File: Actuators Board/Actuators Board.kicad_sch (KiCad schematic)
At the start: 73 parts, among them J1 Conn_01x05_Male, J10 Conn_01x02_Male, J2 Solenoid(Sol), J4 Conn_01x03_Male, J5 Conn_01x06_Male, J9 Conn_01x02_Male, Q1 MMDT2222A, Q2 SI2366DS, U1 ESP32-PICO-D4, U2 TPS54233D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

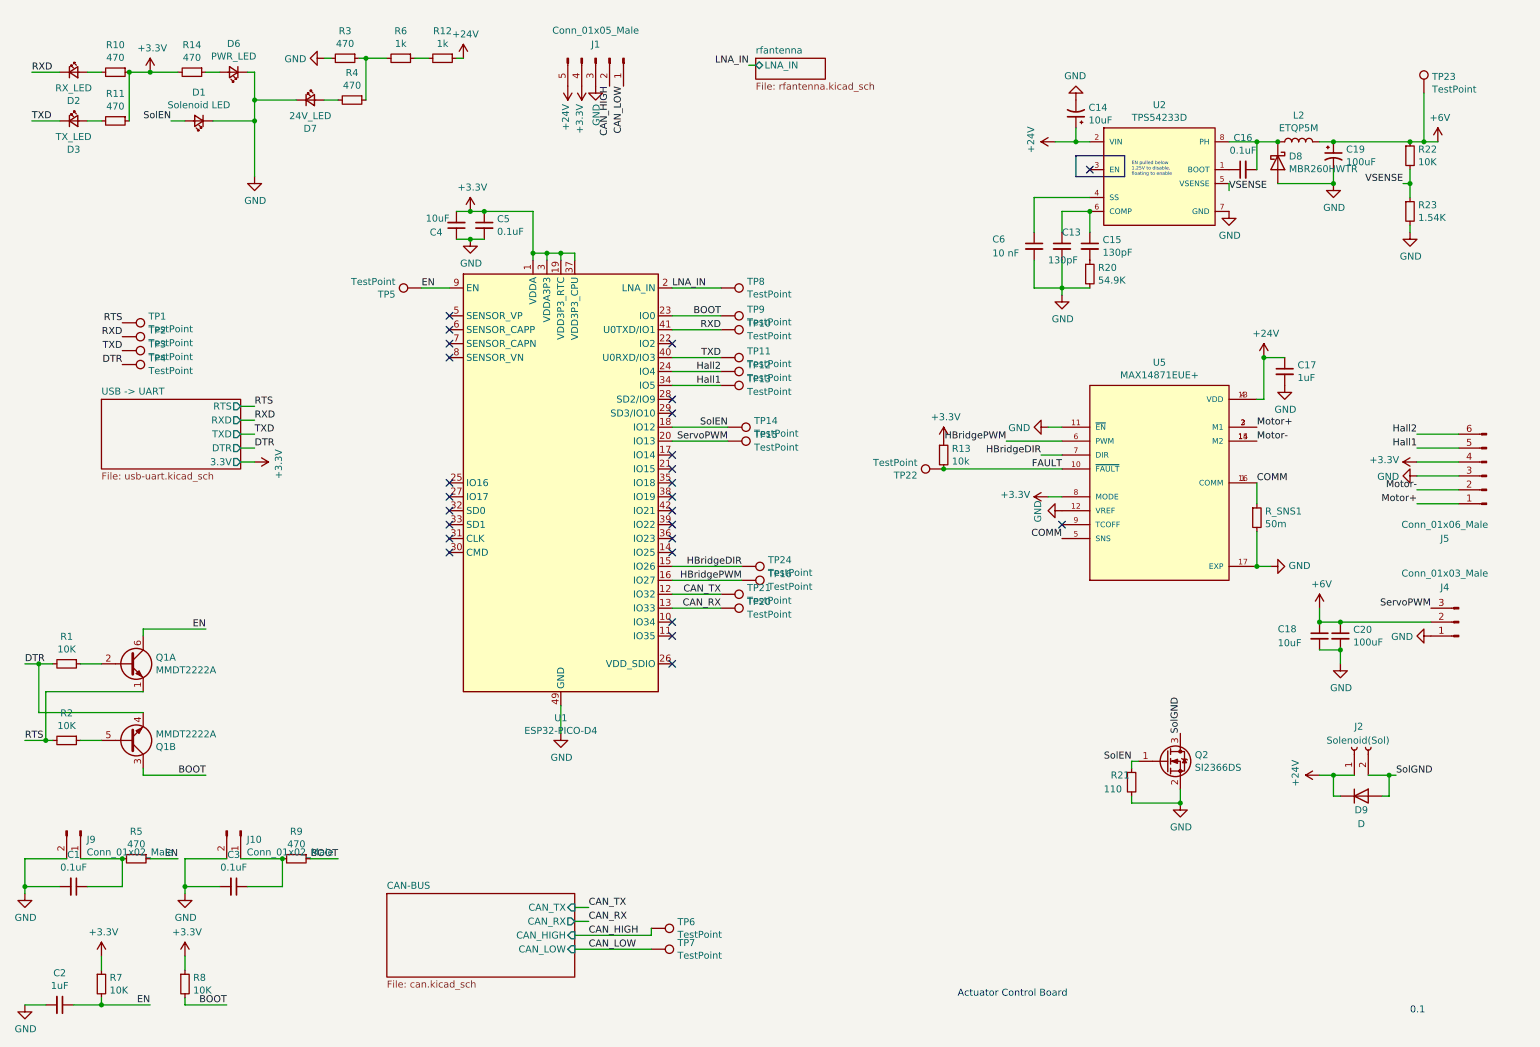
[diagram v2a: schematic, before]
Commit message: Preliminary layout of buck converter & supporting components
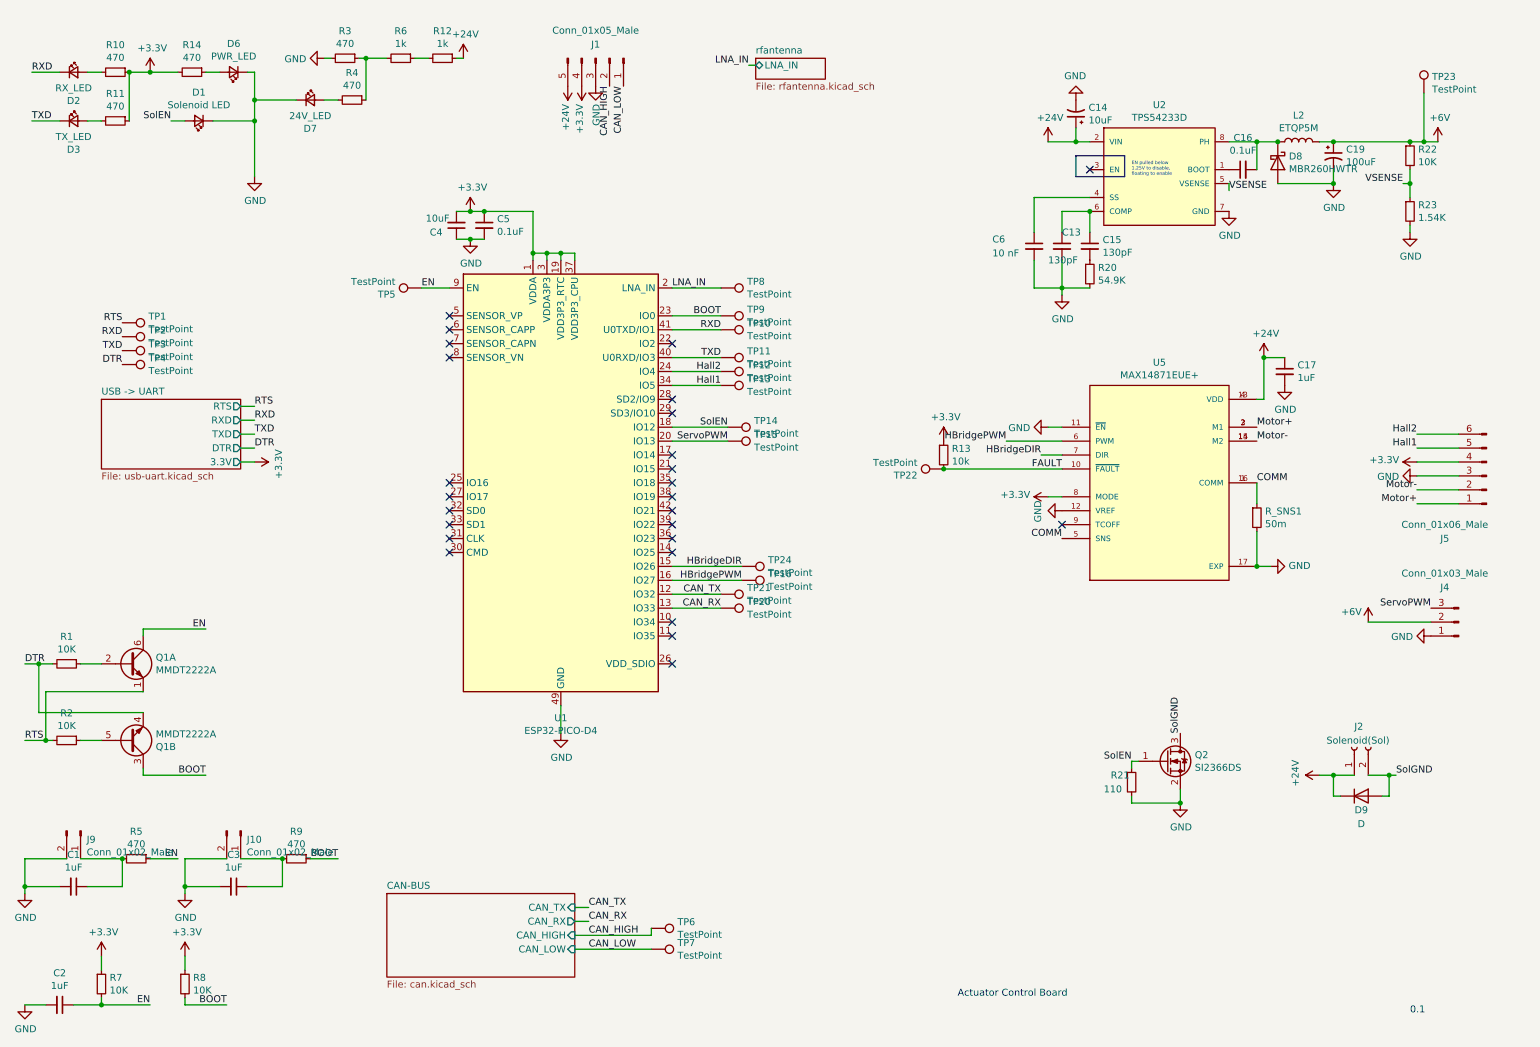
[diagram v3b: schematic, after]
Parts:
- removed C18: 10uF, Capacitor_SMD:C_0603_1608Metric, symbol Device:C_Small
- removed C20: 100uF, Capacitor_SMD:C_0603_1608Metric, symbol Device:C_Small
- C1, C3: value 0.1uF -> 1uF
- J4: footprint (none) -> Connector_JST:JST_XH_B3B-XH-AM_1x03_P2.50mm_Vertical
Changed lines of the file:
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@@
   (junction (at 35.56 21.59) (diameter 0) (color 0 0 0 0)
   )
-  (junction (at 252.73 121.92) (diameter 0) (color 0 0 0 0)
-  )
   (junction (at 241.3 111.76) (diameter 0) (color 0 0 0 0)
   )
@@
   (junction (at 78.74 19.05) (diameter 0) (color 0 0 0 0)
   )
-  (junction (at 256.54 121.92) (diameter 0) (color 0 0 0 0)
-  )
   (junction (at 16.51 170.18) (diameter 0) (color 0 0 0 0)
   )
@@
   )
   (junction (at 97.79 52.07) (diameter 0) (color 0 0 0 0)
-  )
-  (junction (at 256.54 127) (diameter 0) (color 0 0 0 0)
   )
   (junction (at 19.05 129.54) (diameter 0) (color 0 0 0 0)
@@
     (stroke (width 0) (type default) (color 0 0 0 0))
   )
-  (wire (pts (xy 256.54 127) (xy 256.54 129.54))
-    (stroke (width 0) (type default) (color 0 0 0 0))
-  )
   (wire (pts (xy 205.74 60.96) (xy 205.74 62.23))
     (stroke (width 0) (type default) (color 0 0 0 0))
@@
     (stroke (width 0) (type default) (color 0 0 0 0))
   )
-  (wire (pts (xy 208.28 34.29) (xy 204.47 34.29))
+  (wire (pts (xy 208.28 34.29) (xy 203.2 34.29))
     (stroke (width 0) (type default) (color 0 0 0 0))
   )
@@
     (stroke (width 0) (type default) (color 0 0 0 0))
   )
-  (wire (pts (xy 252.73 121.92) (xy 252.73 119.38))
-    (stroke (width 0) (type default) (color 0 0 0 0))
-  )
   (wire (pts (xy 278.13 95.25) (xy 270.51 95.25))
     (stroke (width 0) (type default) (color 0 0 0 0))
@@
     (stroke (width 0) (type default) (color 0 0 0 0))
   )
-  (wire (pts (xy 256.54 121.92) (xy 252.73 121.92))
-    (stroke (width 0) (type default) (color 0 0 0 0))
-  )
   (wire (pts (xy 218.44 153.67) (xy 218.44 154.94))
     (stroke (width 0) (type default) (color 0 0 0 0))
@@
     (stroke (width 0) (type default) (color 0 0 0 0))
   )
-  (wire (pts (xy 252.73 127) (xy 256.54 127))
-    (stroke (width 0) (type default) (color 0 0 0 0))
-  )
   (wire (pts (xy 236.22 34.29) (xy 241.3 34.29))
     (stroke (width 0) (type default) (color 0 0 0 0))
@@
     (stroke (width 0) (type default) (color 0 0 0 0))
   )
-  (wire (pts (xy 273.05 121.92) (xy 256.54 121.92))
+  (wire (pts (xy 273.05 121.92) (xy 261.62 121.92))
     (stroke (width 0) (type default) (color 0 0 0 0))
   )
@@
     (in_bom yes) (on_board yes)
     (property "Reference" "C3" (id 0) (at 54.61 164.3634 90))
-    (property "Value" "0.1uF" (id 1) (at 54.61 166.6748 90))
+    (property "Value" "1uF" (id 1) (at 54.61 166.6748 90))
     (property "Footprint" "Capacitor_SMD:C_0603_1608Metric" (id 2) (at 54.61 170.18 0)
       (effects (font (size 1.27 1.27)) hide)
@@
     (in_bom yes) (on_board yes)
     (property "Reference" "C1" (id 0) (at 25.4 164.3634 90))
-    (property "Value" "0.1uF" (id 1) (at 25.4 166.6748 90))
+    (property "Value" "1uF" (id 1) (at 25.4 166.6748 90))
     (property "Footprint" "Capacitor_SMD:C_0603_1608Metric" (id 2) (at 25.4 170.18 0)
       (effects (font (size 1.27 1.27)) hide)
@@
     (pin "1")
   )
-  (symbol (lib_id "power:+24V") (at 204.47 34.29 90) (unit 1)
-    (in_bom yes) (on_board yes)
-    (property "Reference" "#PWR0104" (id 0) (at 208.28 34.29 0)
-      (effects (font (size 1.27 1.27)) hide)
-    )
-    (property "Value" "+24V" (id 1) (at 200.0758 33.909 0))
-    (property "Footprint" "" (id 2) (at 204.47 34.29 0)
-      (effects (font (size 1.27 1.27)) hide)
-    )
-    (property "Datasheet" "" (id 3) (at 204.47 34.29 0)
+  (symbol (lib_id "power:+24V") (at 203.2 34.29 0) (unit 1)
+    (in_bom yes) (on_board yes)
+    (property "Reference" "#PWR0104" (id 0) (at 203.2 38.1 0)
+      (effects (font (size 1.27 1.27)) hide)
+    )
+    (property "Value" "+24V" (id 1) (at 203.581 29.8958 0))
+    (property "Footprint" "" (id 2) (at 203.2 34.29 0)
+      (effects (font (size 1.27 1.27)) hide)
+    )
+    (property "Datasheet" "" (id 3) (at 203.2 34.29 0)
       (effects (font (size 1.27 1.27)) hide)
     )
@@
     (property "Reference" "J4" (id 0) (at 275.59 115.57 0))
     (property "Value" "Conn_01x03_Male" (id 1) (at 275.59 113.03 0))
-    (property "Footprint" "" (id 2) (at 278.13 121.92 0)
+    (property "Footprint" "Connector_JST:JST_XH_B3B-XH-AM_1x03_P2.50mm_Vertical" (id 2) (at 278.13 121.92 0)
       (effects (font (size 1.27 1.27)) hide)
     )
@@
     (pin "2")
     (pin "3")
-  )
-  (symbol (lib_id "Device:C_Small") (at 256.54 124.46 0) (unit 1)
-    (in_bom yes) (on_board yes)
-    (property "Reference" "C20" (id 0) (at 258.8768 123.2916 0)
-      (effects (font (size 1.27 1.27)) (justify left))
-    )
-    (property "Value" "100uF" (id 1) (at 258.8768 125.603 0)
-      (effects (font (size 1.27 1.27)) (justify left))
-    )
-    (property "Footprint" "Capacitor_SMD:C_0603_1608Metric" (id 2) (at 256.54 124.46 0)
-      (effects (font (size 1.27 1.27)) hide)
-    )
-    (property "Datasheet" "~" (id 3) (at 256.54 124.46 0)
-      (effects (font (size 1.27 1.27)) hide)
-    )
-    (pin "1")
-    (pin "2")
-  )
-  (symbol (lib_id "Device:C_Small") (at 252.73 124.46 0) (unit 1)
-    (in_bom yes) (on_board yes)
-    (property "Reference" "C18" (id 0) (at 245.11 123.19 0)
-      (effects (font (size 1.27 1.27)) (justify left))
-    )
-    (property "Value" "10uF" (id 1) (at 245.11 125.73 0)
-      (effects (font (size 1.27 1.27)) (justify left))
-    )
-    (property "Footprint" "Capacitor_SMD:C_0603_1608Metric" (id 2) (at 252.73 124.46 0)
-      (effects (font (size 1.27 1.27)) hide)
-    )
-    (property "Datasheet" "~" (id 3) (at 252.73 124.46 0)
-      (effects (font (size 1.27 1.27)) hide)
-    )
-    (pin "1")
-    (pin "2")
   )
   (symbol (lib_id "power:+3.3V") (at 97.79 46.99 0) (unit 1)
@@
     (pin "1")
   )
-  (symbol (lib_id "power:GND") (at 256.54 129.54 0) (unit 1)
-    (in_bom yes) (on_board yes)
-    (property "Reference" "#PWR0115" (id 0) (at 256.54 135.89 0)
-      (effects (font (size 1.27 1.27)) hide)
-    )
-    (property "Value" "GND" (id 1) (at 256.667 133.9342 0))
-    (property "Footprint" "" (id 2) (at 256.54 129.54 0)
-      (effects (font (size 1.27 1.27)) hide)
-    )
-    (property "Datasheet" "" (id 3) (at 256.54 129.54 0)
-      (effects (font (size 1.27 1.27)) hide)
-    )
-    (pin "1")
-  )
   (symbol (lib_id "power:GND") (at 273.05 124.46 270) (unit 1)
     (in_bom yes) (on_board yes)
@@
     (pin "1")
   )
-  (symbol (lib_id "power:+6V") (at 252.73 119.38 0) (unit 1)
-    (in_bom yes) (on_board yes)
-    (property "Reference" "#PWR0113" (id 0) (at 252.73 123.19 0)
-      (effects (font (size 1.27 1.27)) hide)
-    )
-    (property "Value" "+6V" (id 1) (at 253.111 114.9858 0))
-    (property "Footprint" "" (id 2) (at 252.73 119.38 0)
-      (effects (font (size 1.27 1.27)) hide)
-    )
-    (property "Datasheet" "" (id 3) (at 252.73 119.38 0)
+  (symbol (lib_id "power:+6V") (at 261.62 121.92 0) (unit 1)
+    (in_bom yes) (on_board yes)
+    (property "Reference" "#PWR0113" (id 0) (at 261.62 125.73 0)
+      (effects (font (size 1.27 1.27)) hide)
+    )
+    (property "Value" "+6V" (id 1) (at 258.5553 120.0478 0))
+    (property "Footprint" "" (id 2) (at 261.62 121.92 0)
+      (effects (font (size 1.27 1.27)) hide)
+    )
+    (property "Datasheet" "" (id 3) (at 261.62 121.92 0)
       (effects (font (size 1.27 1.27)) hide)
     )
@@
       (reference "#PWR0114") (unit 1) (value "GND") (footprint "")
     )
-    (path "/00000000-0000-0000-0000-000061acf34c"
-      (reference "#PWR0115") (unit 1) (value "GND") (footprint "")
-    )
     (path "/00000000-0000-0000-0000-000061bfaac9"
       (reference "#PWR0116") (unit 1) (value "GND") (footprint "")
@@
     )
     (path "/00000000-0000-0000-0000-00005dabbfe7"
-      (reference "C1") (unit 1) (value "0.1uF") (footprint "Capacitor_SMD:C_0603_1608Metric")
+      (reference "C1") (unit 1) (value "1uF") (footprint "Capacitor_SMD:C_0603_1608Metric")
     )
     (path "/00000000-0000-0000-0000-00005da70d8a"
@@
     )
     (path "/00000000-0000-0000-0000-00005dab5946"
-      (reference "C3") (unit 1) (value "0.1uF") (footprint "Capacitor_SMD:C_0603_1608Metric")
+      (reference "C3") (unit 1) (value "1uF") (footprint "Capacitor_SMD:C_0603_1608Metric")
     )
     (path "/00000000-0000-0000-0000-000061aa6786"
@@
       (reference "C17") (unit 1) (value "1uF") (footprint "Capacitor_SMD:C_0603_1608Metric")
     )
-    (path "/00000000-0000-0000-0000-000061aa572c"
-      (reference "C18") (unit 1) (value "10uF") (footprint "Capacitor_SMD:C_0603_1608Metric")
-    )
     (path "/00000000-0000-0000-0000-0000619a1e4e"
       (reference "C19") (unit 1) (value "100uF") (footprint "Capacitor_SMD:CP_Elec_5x5.9")
     )
-    (path "/00000000-0000-0000-0000-000061aa4813"
-      (reference "C20") (unit 1) (value "100uF") (footprint "Capacitor_SMD:C_0603_1608Metric")
-    )
     (path "/00000000-0000-0000-0000-000061db1e33"
       (reference "D1") (unit 1) (value "Solenoid LED") (footprint "LED_SMD:LED_0603_1608Metric")
@@
     )
     (path "/00000000-0000-0000-0000-000061a7be4f"
-      (reference "J4") (unit 1) (value "Conn_01x03_Male") (footprint "")
+      (reference "J4") (unit 1) (value "Conn_01x03_Male") (footprint "Connector_JST:JST_XH_B3B-XH-AM_1x03_P2.50mm_Vertical")
     )
     (path "/00000000-0000-0000-0000-000061bfaac3"
